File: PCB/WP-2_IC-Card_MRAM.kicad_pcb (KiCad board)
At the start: 2 copper layers, 54 x 54 mm, 37 parts, among them J1 SMS-138-01-G-S, SW1 CUS-14TB, U1 MRxA08xxYSxxx, U2 MIC5317-3.3YD5, U3 4245, U4 4245, U5 4245, U6 4245

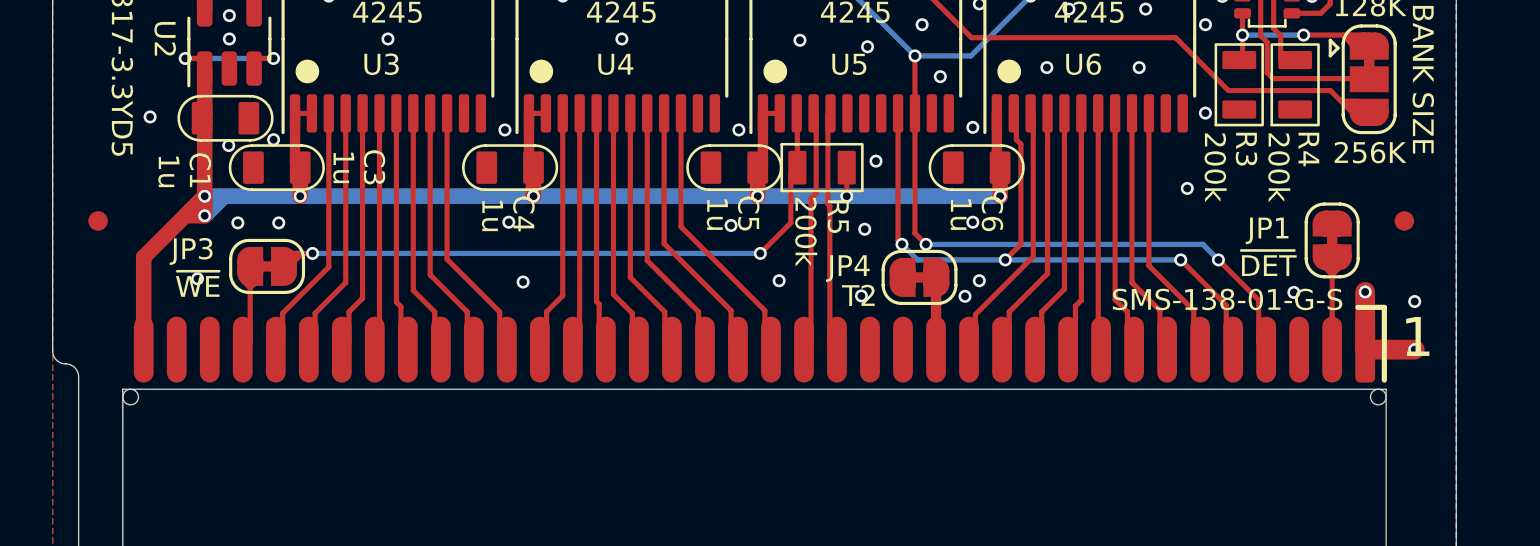
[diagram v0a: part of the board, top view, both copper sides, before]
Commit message: 4 symmetric fiducials
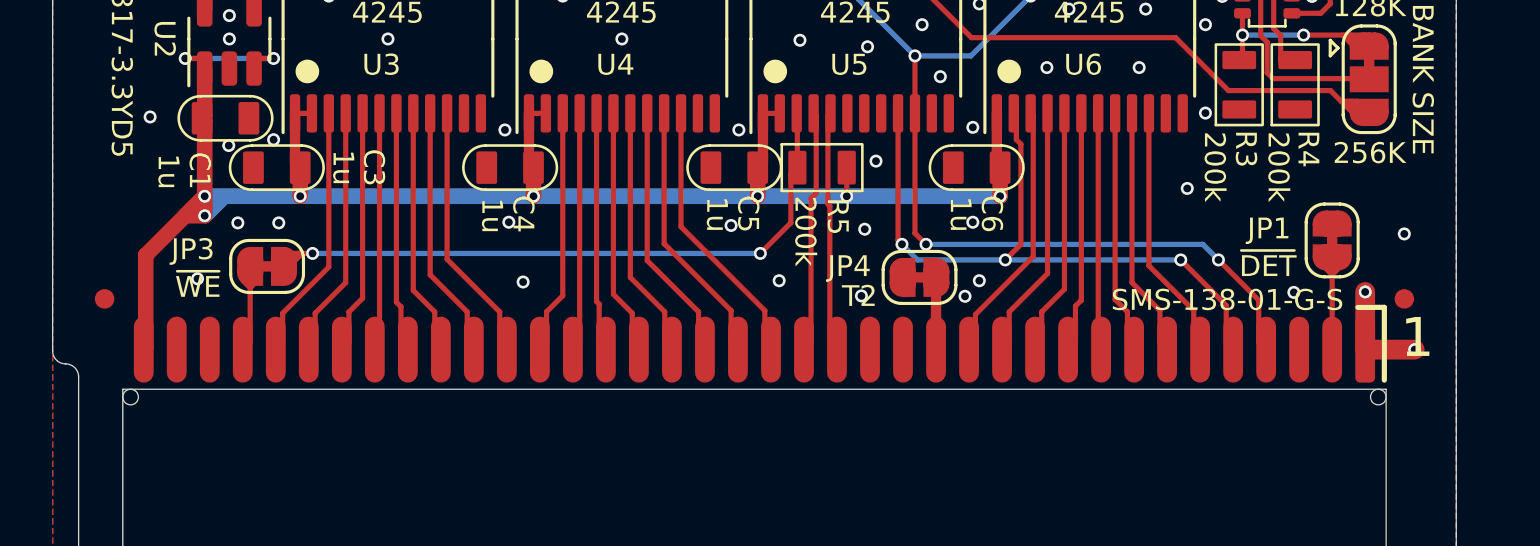
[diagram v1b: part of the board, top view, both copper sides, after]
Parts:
- moved REF** 3.01 mm to (111.0, 110.2)
- moved REF** 3.00 mm to (160.9, 110.2)

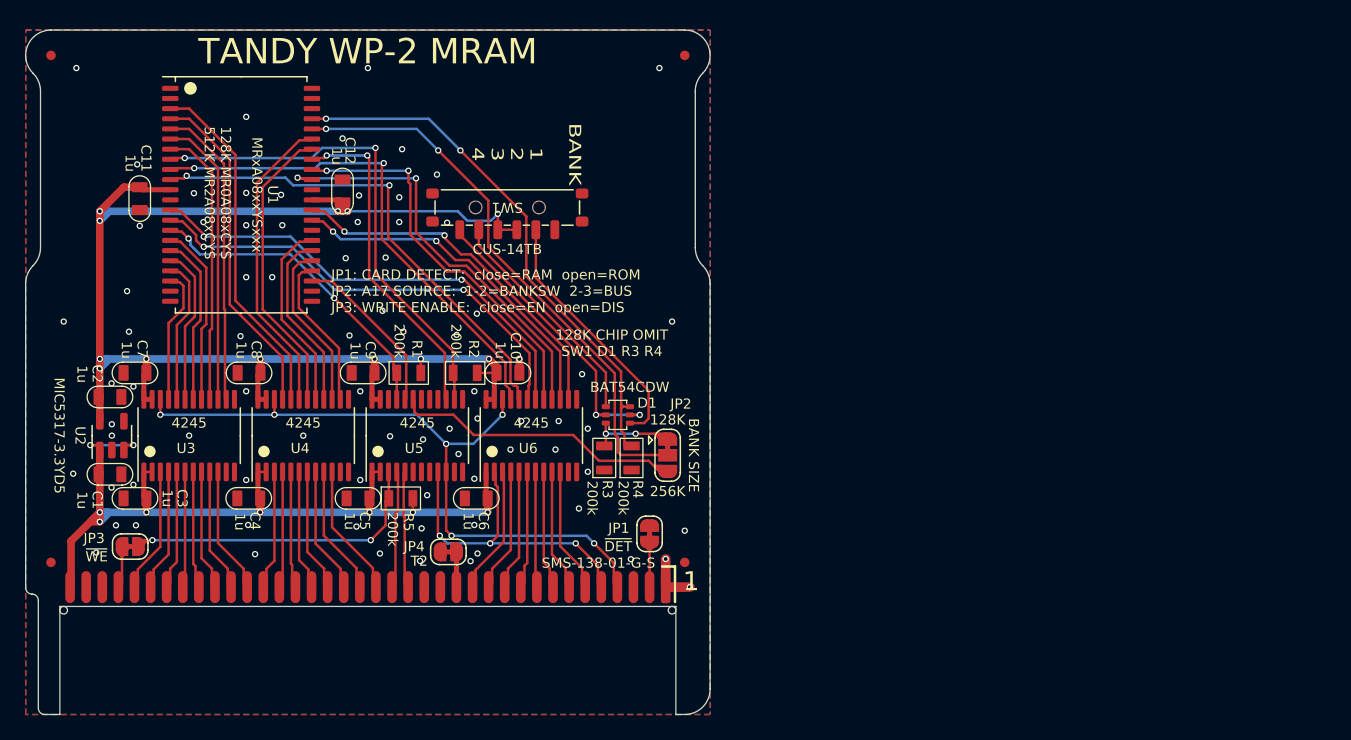
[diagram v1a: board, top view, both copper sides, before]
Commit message: mram bav74 diodes
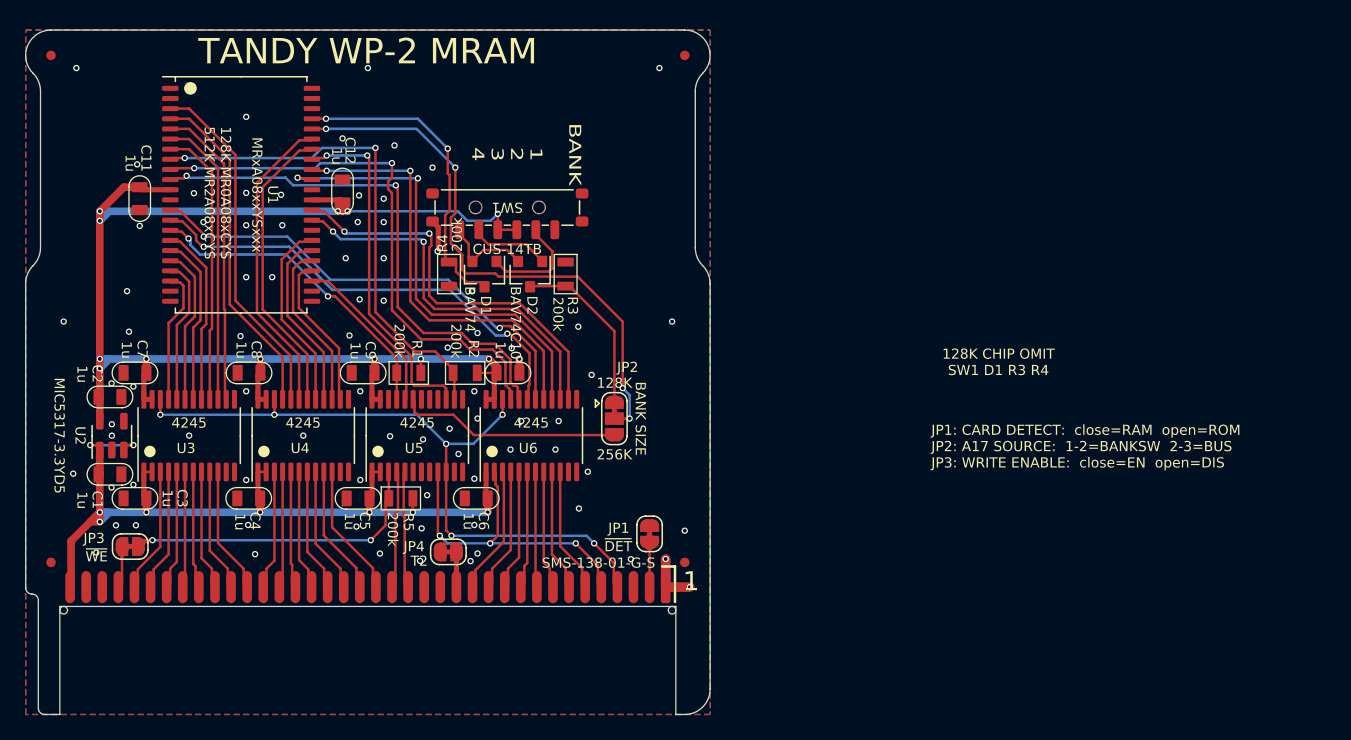
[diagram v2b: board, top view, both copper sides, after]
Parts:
- added D2: BAV74, 000_LOCAL:SOT-23, F.Cu at (148.8, 87.5)
- D1: value BAT54CDW -> BAV74; footprint 000_LOCAL:TSSOP-6-symmetric -> 000_LOCAL:SOT-23
- moved R4 20.4 mm to (142.3, 87.5)
- moved D1 15.3 mm to (145.2, 87.5), turned to -90 degrees
- moved R3 14.8 mm to (151.6, 87.5), turned to -90 degrees
- moved JP2 5.10 mm to (155.4, 98.9)
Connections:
- D1 pad 1: /BANK_3 -> /BANK_2
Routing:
- net /3A18: track 43.0 -> 25.1 mm
- net /BANK_4: track 24.1 -> 7.47 mm, vias 2 -> 0
- net /BANK_3: track 18.1 -> 6.30 mm
- net /BANK_2: track 20.2 -> 8.45 mm
- net /3A17bank: track 7.10 -> 13.7 mm, vias 2 -> 0
- net /3A17bus: track 23.0 -> 17.6 mm
- net /3D0: track 40.0 -> 43.3 mm
- net /3D6: track 33.2 -> 36.5 mm
- net /3D7: track 30.9 -> 34.1 mm
- net /3D1: track 39.0 -> 42.0 mm
- net /3D5: track 28.7 -> 31.6 mm
- net /3D4: track 27.6 -> 30.3 mm
- net GND: track 5.22 -> 7.78 mm, vias 80 -> 82
- net /~{3OE}: track 26.3 -> 27.7 mm
- net /~{3CE}: track 39.0 -> 39.9 mm
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
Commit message: mram cover new banksw diodes
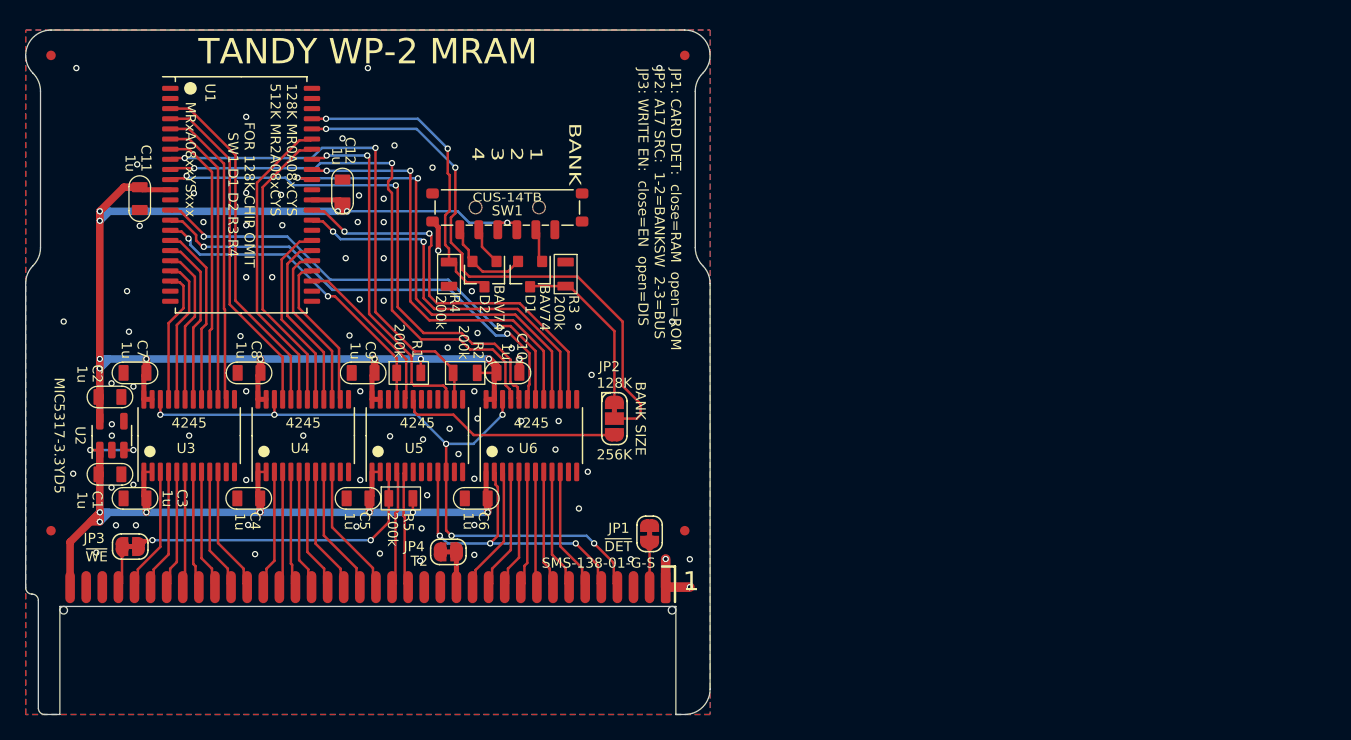
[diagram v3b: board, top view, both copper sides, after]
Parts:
- moved D1 3.60 mm to (148.8, 87.5)
- moved D2 3.60 mm to (145.2, 87.5)
- moved REF** 2.50 mm to (160.9, 107.7)
- moved REF** 2.50 mm to (111.0, 107.7)
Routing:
- net /BANK_2: track 8.45 -> 2.71 mm
- net /BANK_3: track 6.30 -> 3.08 mm
- net VMEM: track 112.0 -> 109.9 mm
- net /3A17: track 44.6 -> 45.6 mm, vias 4 -> 2
- net GND: track 7.78 -> 7.71 mm, vias 82 -> 81
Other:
- board text added: "FOR 128K CHIP OMIT SW1 D1 D2 R3 R4"
- board text added: "JP1: CARD DET: close=RAM open=ROM JP2: A17 SRC: 1-2=BANKSW 2-3=BUS JP3: WRITE EN: close=EN open=DIS"
- board text removed: "128K CHIP OMIT SW1 D1 R3 R4"
- board text removed: "JP1: CARD DETECT: close=RAM open=ROM JP2: A17 SOURCE: 1-2=BANKSW 2-3=BUS JP3: WRITE ENABLE: close=EN open=DIS"

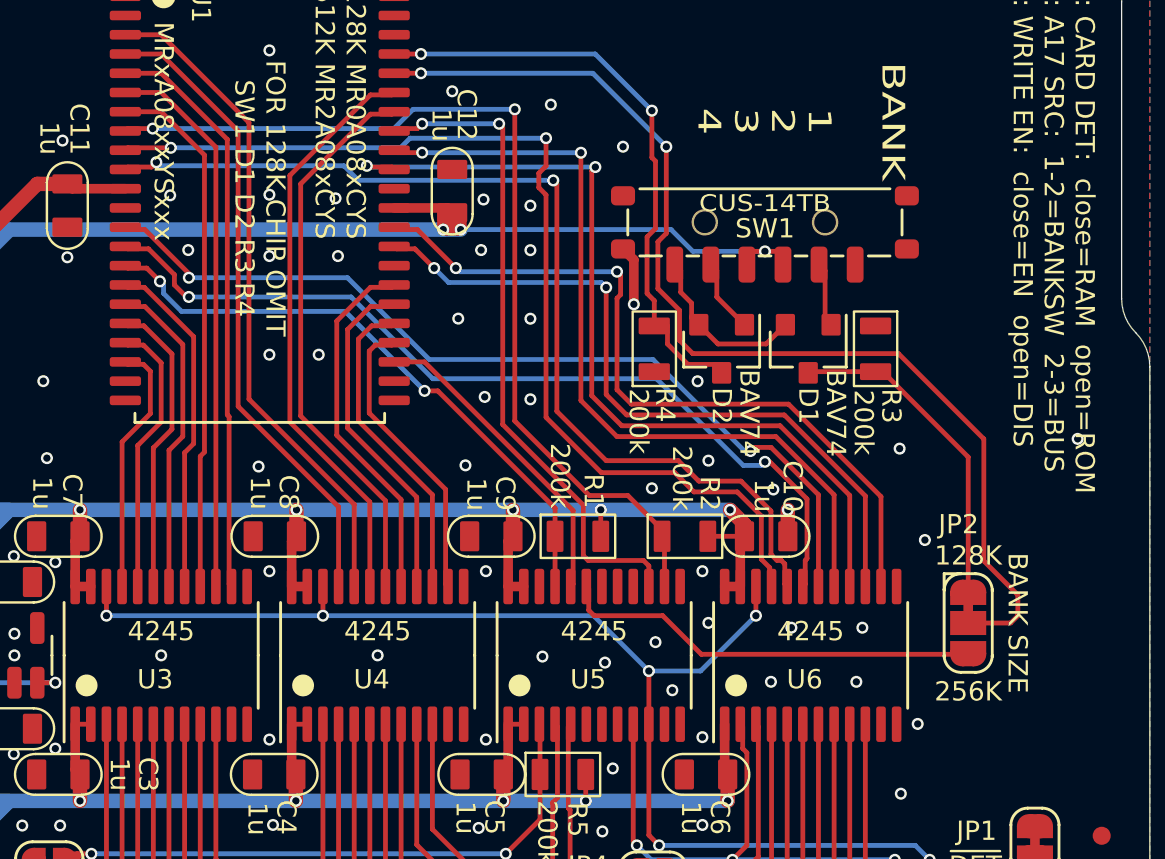
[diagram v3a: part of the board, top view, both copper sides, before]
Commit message: adhesive tape, pics, tiny routing nudges, tsop2-44 model, grid alignment
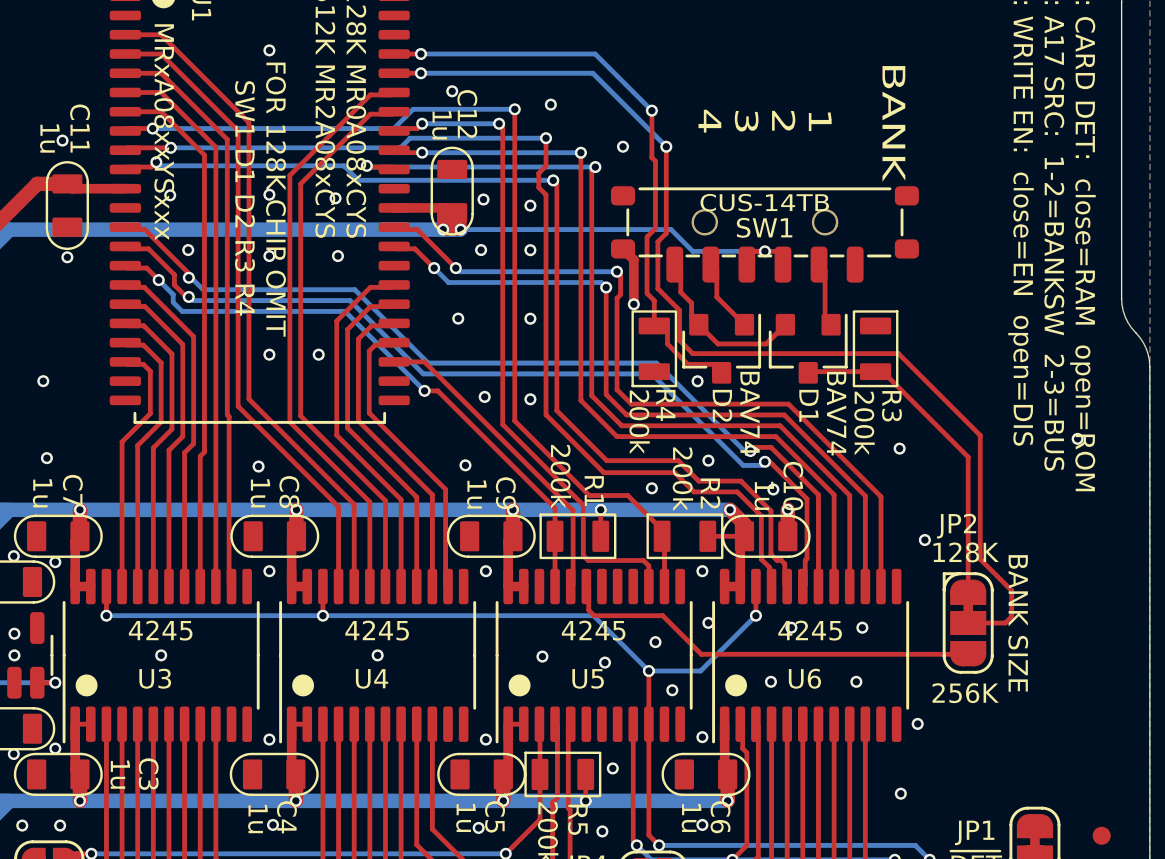
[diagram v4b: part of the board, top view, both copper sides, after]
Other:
- board text added: "5 x ADHESIVE TRANSFER 3MM x 42MM"

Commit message: pics
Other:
- board text added: "3MM ADHESIVE TRANSFER TAPE"
- board text removed: "5 x ADHESIVE TRANSFER 3MM x 42MM"

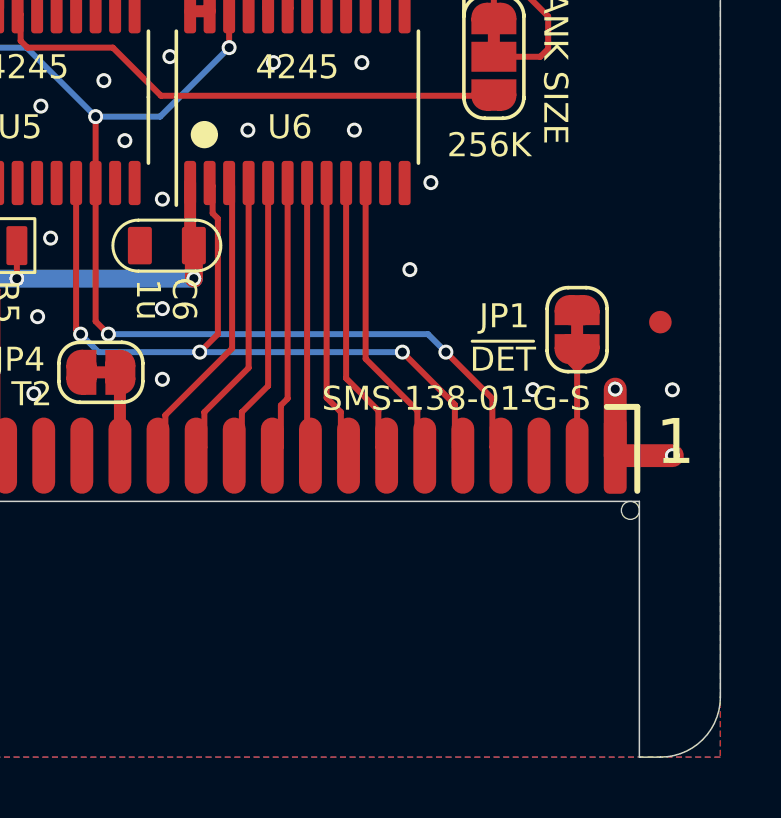
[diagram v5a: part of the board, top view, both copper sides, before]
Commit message: mram silkscreen
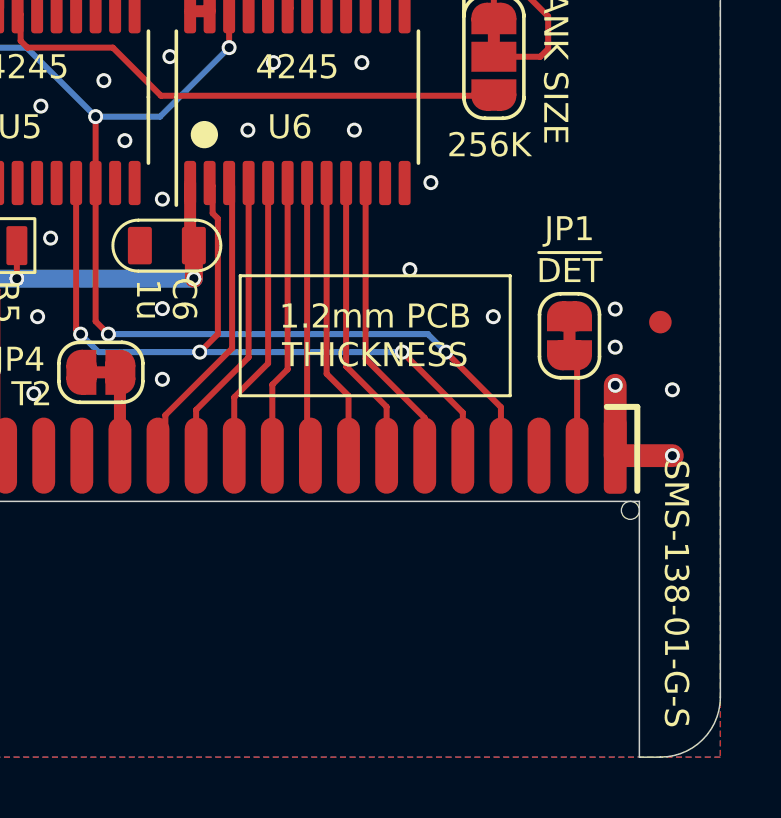
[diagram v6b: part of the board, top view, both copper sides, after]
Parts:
- moved JP1 0.33 mm to (157.9, 108.2)
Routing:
- net GND: track 7.71 -> 7.84 mm, vias 81 -> 83
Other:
- board text added: "1.2mm PCB THICKNESS"
- board text removed: "EXPOSED"
